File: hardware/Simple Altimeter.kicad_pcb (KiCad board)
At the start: 4 copper layers, 15.2 x 27.7 mm, 32 parts, among them J1 USB_C_Receptacle_USB2.0, J2 Conn_01x05_Pin, SW1 SW_Push, U2 BMP280, U3 W25Q16JVUXIQ, U4 STM32F042G6Ux

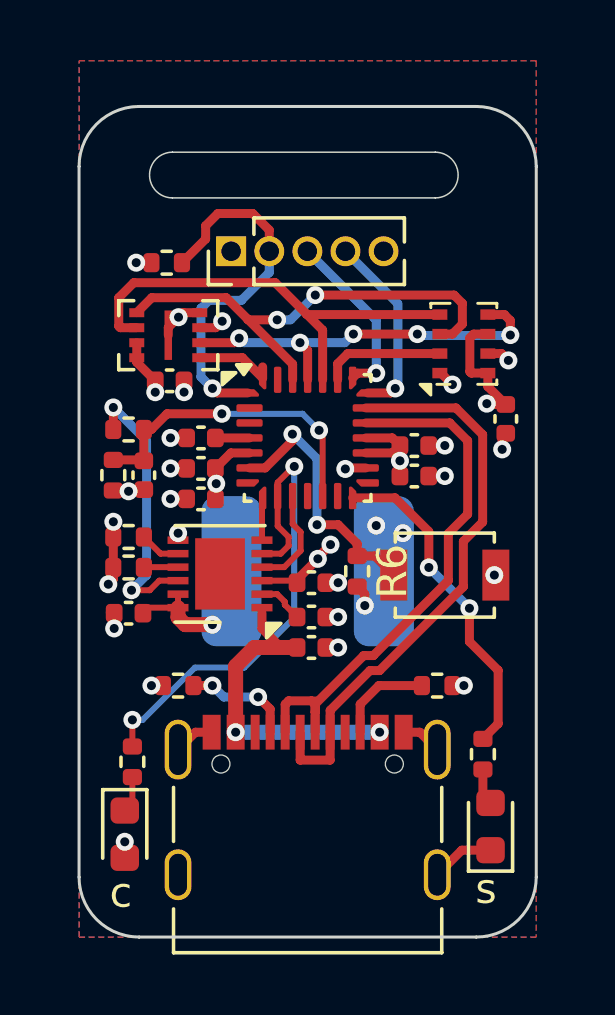
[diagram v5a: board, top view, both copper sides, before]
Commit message: Added power off method for debug, and updated operation.md for new hardware. Cleaned up production files.
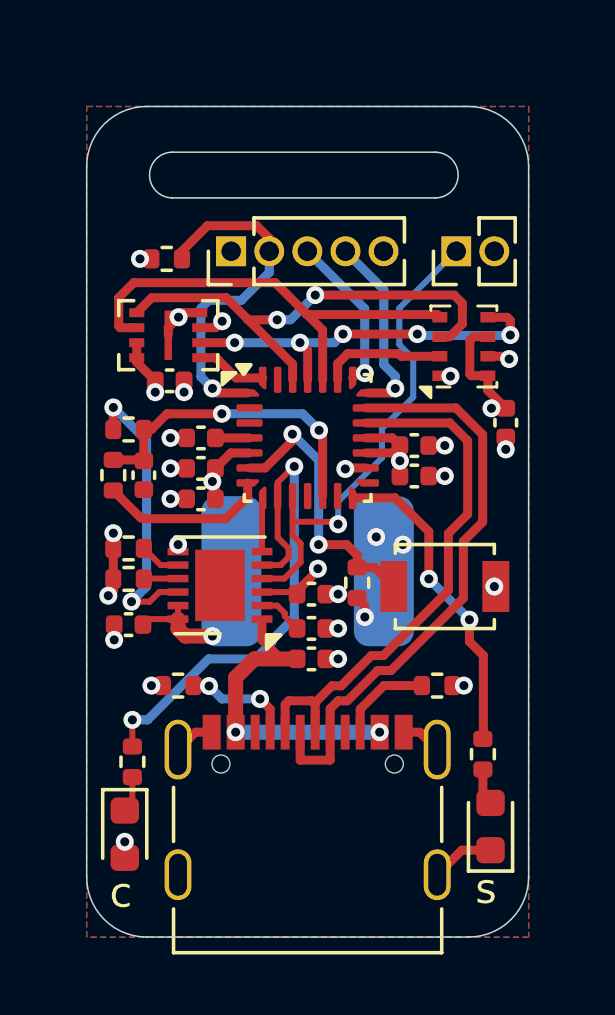
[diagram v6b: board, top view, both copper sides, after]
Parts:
- added J3: Conn_01x02_Pin, Connector_PinHeader_1.27mm:PinHeader_1x02_P1.27mm_Vertical, F.Cu at (154.3, 103.4)
- C1: value 4u7 -> 2u2
- C7: value 1u -> 2u2
- moved C1 0.38 mm to (149.5, 116.0)
- moved C11 0.38 mm to (149.5, 114.8)
- moved C3 0.38 mm to (143.4, 115.8)
- moved C7 0.38 mm to (149.5, 117.0)
- moved R3 0.38 mm to (143.4, 114.3)
- moved R4 0.38 mm to (143.4, 113.3)
- moved R6 0.38 mm to (151.0, 114.4)
- moved SW1 0.38 mm to (153.9, 114.6)
- moved U7 0.38 mm to (146.4, 114.5)
- moved C5 0.13 mm to (156.0, 109.1)
- moved R14 0.13 mm to (144.7, 103.6)
- moved U2 0.09 mm to (154.6, 106.6)
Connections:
- R2 pad 2: GND -> /~{SENSE_EN}
- U4 pad 7: unconnected-(U4-PA1-Pad7) -> /~{SENSE_EN}
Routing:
- net /SHUTDOWN: track 3.45 -> 16.5 mm, vias 0 -> 1
- net /~{SENSE_EN}: track 0.00 -> 5.63 mm
- net GND: track 19.3 -> 17.6 mm, vias 25 -> 24
- net +3.3V: track 16.5 -> 15.5 mm, vias 9 -> 8
- net /BOOT: track 12.3 -> 11.7 mm
- net /SWDCLK: track 5.87 -> 5.33 mm
- net /BUTTON: track 8.88 -> 9.40 mm
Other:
- board size 15.2 x 27.7 mm -> 14.7 x 27.7 mm

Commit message: fixed footprint for W25Q16JVU
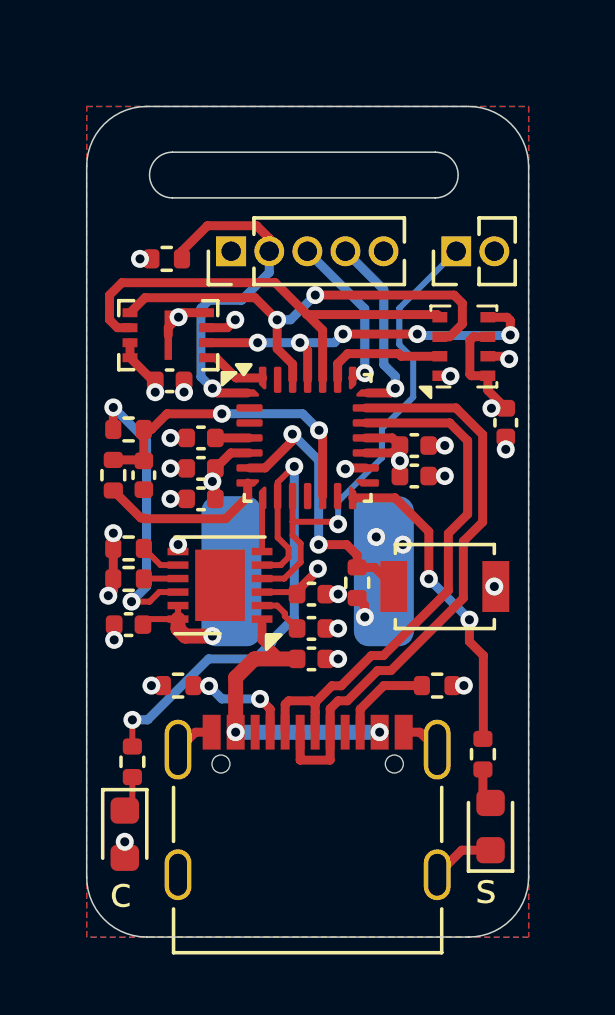
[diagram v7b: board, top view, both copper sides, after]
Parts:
- D2: value RED LED -> GREEN LED
- U7: value ~ -> SNTS01
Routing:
- net /FLASH_~{CS}: track 2.38 -> 1.84 mm

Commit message: Updated component 3d models and regenerated render.
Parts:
- U7: value SNTS01 -> STNS01
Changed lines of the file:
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@@
         (effects (font (size 1 1) (thickness 0.15)))
     )
-    (fp_text value "SNTS01" (at 0 2.55) (layer "F.Fab")
+    (fp_text value "STNS01" (at 0 2.55) (layer "F.Fab")
         (effects (font (size 1 1) (thickness 0.15)))
     )
@@
     (pad "9" smd rect (at 0 0 180) (size 0.25 1.65) (layers "F.Cu" "F.Paste" "F.Mask")
       (net 2 "GND") (pinfunction "EP") (pintype "passive") (thermal_bridge_angle 45))
+    (model ":KICAD7_3DMODEL_DIR:Package_DFN_QFN.3dshapes/DFN-8-1EP_3x2mm_P0.45mm_EP1.66x1.36mm.wrl"
+      (offset (xyz 0 0 0))
+      (scale (xyz 1 1 1))
+      (rotate (xyz 0 0 0))
+    )
   )
   (footprint "Package_DFN_QFN:QFN-28_4x4mm_P0.5mm" (layer "F.Cu")
@@
       (scale (xyz 1 1 1))
       (rotate (xyz 0 0 0))
+    )
+    (model ":KICAD7_3DMODEL_DIR:Connector_USB.3dshapes/USB_C_Receptacle_GCT_USB4105-xx-A_16P_TopMnt_Horizontal.step"
+      (offset (xyz 0 -1.4 0))
+      (scale (xyz 1 1 1))
+      (rotate (xyz 0 0 0))
